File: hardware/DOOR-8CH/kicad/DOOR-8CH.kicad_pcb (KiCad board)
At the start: 4 copper layers, 260 x 160 mm, 209 parts, among them J1 FUSED_12V_CH1, J10 ACTUATOR_CH2, J11 ACTUATOR_CH3, J12 ACTUATOR_CH4, J13 ACTUATOR_CH5, J14 ACTUATOR_CH6, J15 ACTUATOR_CH7, J16 ACTUATOR_CH8, J2 FUSED_12V_CH2, J201 REED_A_OPEN_3V3_SIG_GND, J202 REED_A_CLOSED_3V3_SIG_GND, J203 REED_A_IN_PLACE_3V3_SIG_GND, J204 REED_B_OPEN_3V3_SIG_GND, J205 REED_B_CLOSED_3V3_SIG_GND, J206 REED_B_IN_PLACE_3V3_SIG_GND, J211 CAP_CS1_GND, J212 CAP_CS2_GND, J213 CAP_CS3_GND, J214 CAP_CS4_GND, J215 CAP_CS5_GND, J216 CAP_CS6_GND, J217 CAP_CS7_GND, J218 CAP_CS8_GND, J220 SWD_S1_3V3_DIO_CLK_NRST_GND, J230 LOGIC_12V_GND, J3 FUSED_12V_CH3, J4 FUSED_12V_CH4, J5 FUSED_12V_CH5, J6 FUSED_12V_CH6, J7 FUSED_12V_CH7, J8 FUSED_12V_CH8, J9 ACTUATOR_CH1, U1 VNH5019A-E, U2 VNH5019A-E, U3 VNH5019A-E, U4 VNH5019A-E, U5 VNH5019A-E, U6 VNH5019A-E, U7 VNH5019A-E, U8 VNH5019A-E

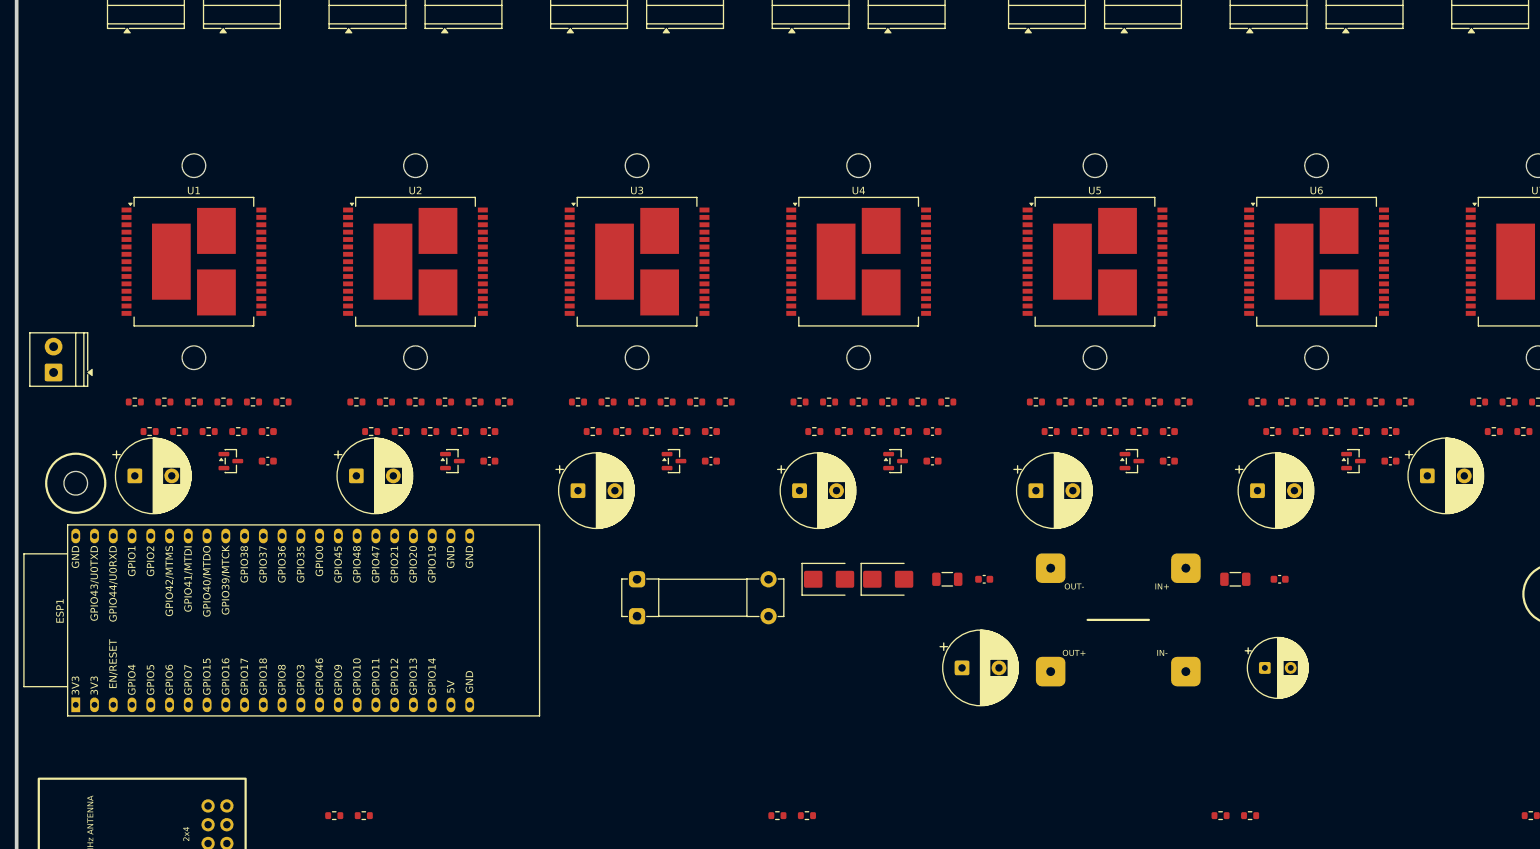
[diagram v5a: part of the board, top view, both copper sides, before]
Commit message: Add DOOR-8CH low-voltage nets
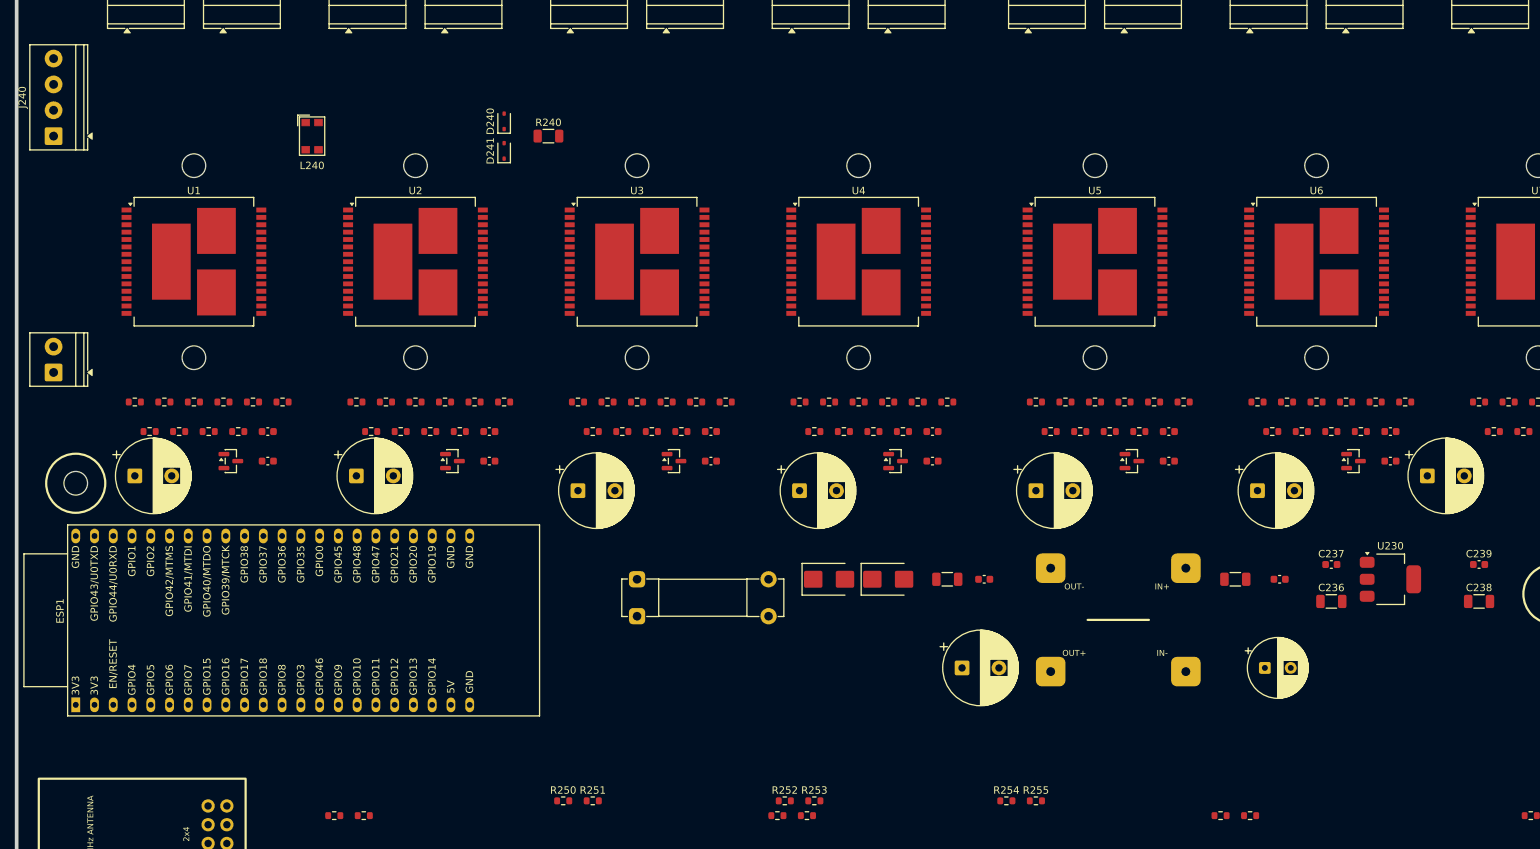
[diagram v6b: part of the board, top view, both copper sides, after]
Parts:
- added C236: 10UF_10V_3V3_IN, C_1206_3216Metric, F.Cu at (178.0, 91.0)
- added C237: 100NF_16V_3V3_IN, C_0603_1608Metric, F.Cu at (178.0, 86.0)
- added C238: 10UF_10V_3V3_OUT, C_1206_3216Metric, F.Cu at (198.0, 91.0)
- added C239: 100NF_16V_3V3_OUT, C_0603_1608Metric, F.Cu at (198.0, 86.0)
- added D240: PESD1CAN_CANH, D_SOD-323, F.Cu at (66.0, 26.0)
- added D241: PESD1CAN_CANL, D_SOD-323, F.Cu at (66.0, 30.0)
- added J240: CANH_CANL_GND_SHIELD, TerminalBlock_Phoenix_PT-1,5-4-3.5-H_1x04_P3.50mm_Horizontal, F.Cu at (5.00, 28.0)
- added L240: CMC_CAN, L_CommonModeChoke_Coilcraft_1812CAN, F.Cu at (40.0, 28.0)
- added R240: 120R_CAN_TERM_DNP, R_1206_3216Metric, F.Cu at (72.0, 28.0)
- added R250: 100R_UART_TX, R_0603_1608Metric, F.Cu at (74.0, 118.0)
- added R251: 100R_UART_TX, R_0603_1608Metric, F.Cu at (78.0, 118.0)
- added R252: 100R_UART_TX, R_0603_1608Metric, F.Cu at (104.0, 118.0)
- added R253: 100R_UART_TX, R_0603_1608Metric, F.Cu at (108.0, 118.0)
- added R254: 100R_UART_TX, R_0603_1608Metric, F.Cu at (134.0, 118.0)
- added R255: 100R_UART_TX, R_0603_1608Metric, F.Cu at (138.0, 118.0)
- added U230: AMS1117-3V3, SOT-223-3_TabPin2, F.Cu at (186.0, 88.0)
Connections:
- C230 pad 1: (no net) -> LOGIC_12V_PROTECTED
- C230 pad 2: (no net) -> GND
- C231 pad 1: (no net) -> LOGIC_12V_PROTECTED
- C231 pad 2: (no net) -> GND
- C232 pad 1: (no net) -> LOGIC_12V_PROTECTED
- C232 pad 2: (no net) -> GND
- C233 pad 1: (no net) -> LOGIC_5V
- C233 pad 2: (no net) -> GND
- C234 pad 1: (no net) -> LOGIC_5V
- C234 pad 2: (no net) -> GND
- C235 pad 1: (no net) -> LOGIC_5V
- C235 pad 2: (no net) -> GND
- CAN1 pad 1: (no net) -> LOGIC_3V3
- CAN1 pad 2: (no net) -> GND
- CAN1 pad 3: (no net) -> S1_CAN_TX
- CAN1 pad 4: (no net) -> S1_CAN_RX
- CAN1 pad 5: (no net) -> CANH_BUS
- CAN1 pad 6: (no net) -> CANL_BUS
- CAN2 pad 1: (no net) -> LOGIC_3V3
- CAN2 pad 2: (no net) -> GND
- CAN2 pad 3: (no net) -> ESP_CAN_TX_GPIO39
- CAN2 pad 4: (no net) -> ESP_CAN_RX_GPIO38
- CAN2 pad 5: (no net) -> CANH_BUS
- CAN2 pad 6: (no net) -> CANL_BUS
- CAP1 pad 1: (no net) -> CAP_MISO
- CAP1 pad 14: (no net) -> CAP_MOSI
- CAP1 pad 15: (no net) -> CAP_CS
- CAP1 pad 16: (no net) -> CAP_RESET
- CAP1 pad 18: (no net) -> CAP_C1_RAW
- CAP1 pad 19: (no net) -> CAP_C2_RAW
- CAP1 pad 2: (no net) -> CAP_SCK
- CAP1 pad 20: (no net) -> CAP_C3_RAW
- CAP1 pad 21: (no net) -> CAP_C4_RAW
- CAP1 pad 22: (no net) -> CAP_C5_RAW
- CAP1 pad 23: (no net) -> CAP_C6_RAW
- CAP1 pad 24: (no net) -> CAP_C7_RAW
- CAP1 pad 25: (no net) -> CAP_C8_RAW
- CAP1 pad 26: (no net) -> GND
- CAP1 pad 3: (no net) -> LOGIC_5V
- CAP1 pad 4: (no net) -> GND
- D230 pad 1: (no net) -> LOGIC_12V_FUSED
- D230 pad 2: (no net) -> LOGIC_12V_PROTECTED
- D231 pad 1: (no net) -> LOGIC_12V_PROTECTED
- D231 pad 2: (no net) -> GND
- DC1 pad 1: (no net) -> LOGIC_12V_PROTECTED
- DC1 pad 2: (no net) -> GND
- DC1 pad 3: (no net) -> LOGIC_5V
- DC1 pad 4: (no net) -> GND
- ESP1 pad 15: (no net) -> RF_LEARN_BUTTON_GPIO9
- ESP1 pad 16: (no net) -> RF_CSN
- ESP1 pad 17: (no net) -> RF_MOSI
- ESP1 pad 18: (no net) -> RF_SCK
- ESP1 pad 19: (no net) -> RF_MISO
- ESP1 pad 21: (no net) -> LOGIC_5V
- ESP1 pad 22: (no net) -> GND
- ESP1 pad 23: (no net) -> GND
- ESP1 pad 24: (no net) -> GND
- ESP1 pad 35: (no net) -> ESP_CAN_RX_GPIO38
- ESP1 pad 36: (no net) -> ESP_CAN_TX_GPIO39
- ESP1 pad 4: (no net) -> RF_GDO0
- ESP1 pad 44: (no net) -> GND
- ESP1 pad 5: (no net) -> RF_GDO2
- F230 pad 1: (no net) -> LOGIC_12V_IN
- F230 pad 2: (no net) -> LOGIC_12V_FUSED
- J201 pad 1: (no net) -> S1_3V3
- J201 pad 2: (no net) -> REED_A_OPEN
- J201 pad 3: (no net) -> GND
- J202 pad 1: (no net) -> S1_3V3
- J202 pad 2: (no net) -> REED_A_CLOSED
- J202 pad 3: (no net) -> GND
- J203 pad 1: (no net) -> S1_3V3
- J203 pad 2: (no net) -> REED_A_IN_PLACE
- J203 pad 3: (no net) -> GND
- J204 pad 1: (no net) -> S2_3V3
- J204 pad 2: (no net) -> REED_B_OPEN
- J204 pad 3: (no net) -> GND
- J205 pad 1: (no net) -> S2_3V3
- J205 pad 2: (no net) -> REED_B_CLOSED
- J205 pad 3: (no net) -> GND
- J206 pad 1: (no net) -> S2_3V3
- J206 pad 2: (no net) -> REED_B_IN_PLACE
- J206 pad 3: (no net) -> GND
- J211 pad 1: (no net) -> CAP_C1_FIELD
- J211 pad 2: (no net) -> GND
- J212 pad 1: (no net) -> CAP_C2_FIELD
- J212 pad 2: (no net) -> GND
- J213 pad 1: (no net) -> CAP_C3_FIELD
- J213 pad 2: (no net) -> GND
- J214 pad 1: (no net) -> CAP_C4_FIELD
- J214 pad 2: (no net) -> GND
- J215 pad 1: (no net) -> CAP_C5_FIELD
- J215 pad 2: (no net) -> GND
- J216 pad 1: (no net) -> CAP_C6_FIELD
- J216 pad 2: (no net) -> GND
- J217 pad 1: (no net) -> CAP_C7_FIELD
- J217 pad 2: (no net) -> GND
- J218 pad 1: (no net) -> CAP_C8_FIELD
- J218 pad 2: (no net) -> GND
- J220 pad 1: (no net) -> S1_3V3
- J220 pad 2: (no net) -> S1_SWDIO
- J220 pad 3: (no net) -> S1_SWCLK
- J220 pad 4: (no net) -> S1_NRST
- J220 pad 5: (no net) -> GND
- J230 pad 1: (no net) -> LOGIC_12V_IN
- J230 pad 2: (no net) -> GND
- MOD1 pad 13: (no net) -> CAP_IRQ
- MOD1 pad 14: (no net) -> S1_UART3_RX
- MOD1 pad 16: (no net) -> S1_NRST
- MOD1 pad 17: (no net) -> CAP_MISO
- MOD1 pad 18: (no net) -> CAP_CS
- MOD1 pad 19: (no net) -> S1_UART2_TX
- MOD1 pad 24: (no net) -> S1_CAN_TX
- MOD1 pad 25: (no net) -> S1_SWCLK
- MOD1 pad 28: (no net) -> S1_UART1_RX
- MOD1 pad 29: (no net) -> CAP_RESET
- MOD1 pad 33: (no net) -> S1_CAN_RX
- MOD1 pad 34: (no net) -> S1_SWDIO
- MOD1 pad 37: (no net) -> S1_UART1_TX
- MOD1 pad 38: (no net) -> REED_A_IN_PLACE
- MOD1 pad 4: (no net) -> S1_UART3_TX
- MOD1 pad 5: (no net) -> REED_A_CLOSED
- MOD1 pad 6: (no net) -> REED_A_OPEN
- MOD1 pad 7: S1_SLOT_ID1 -> CAP_MOSI
- MOD1 pad 8: (no net) -> CAP_SCK
- MOD1 pad 9: (no net) -> S1_UART2_RX
- MOD2 pad 28: (no net) -> S2_UART_RX
- MOD2 pad 37: (no net) -> S2_UART_TX
- MOD2 pad 38: (no net) -> REED_B_IN_PLACE
- MOD2 pad 5: (no net) -> REED_B_CLOSED
- MOD2 pad 6: (no net) -> REED_B_OPEN
- MOD3 pad 28: (no net) -> S3_UART_RX
- MOD3 pad 37: (no net) -> S3_UART_TX
- MOD4 pad 28: (no net) -> S4_UART_RX
- MOD4 pad 37: (no net) -> S4_UART_TX
- R201 pad 1: (no net) -> CAP_C1_RAW
- R201 pad 2: (no net) -> CAP_C1_FIELD
- R202 pad 1: (no net) -> CAP_C2_RAW
- R202 pad 2: (no net) -> CAP_C2_FIELD
- R203 pad 1: (no net) -> CAP_C3_RAW
- R203 pad 2: (no net) -> CAP_C3_FIELD
- R204 pad 1: (no net) -> CAP_C4_RAW
- R204 pad 2: (no net) -> CAP_C4_FIELD
- R205 pad 1: (no net) -> CAP_C5_RAW
- R205 pad 2: (no net) -> CAP_C5_FIELD
- R206 pad 1: (no net) -> CAP_C6_RAW
- R206 pad 2: (no net) -> CAP_C6_FIELD
- R207 pad 1: (no net) -> CAP_C7_RAW
- R207 pad 2: (no net) -> CAP_C7_FIELD
- R208 pad 1: (no net) -> CAP_C8_RAW
- R208 pad 2: (no net) -> CAP_C8_FIELD
- R209 pad 1: (no net) -> CAP_RESET
- R209 pad 2: (no net) -> GND
- R210 pad 1: (no net) -> CAP_IRQ
- R210 pad 2: (no net) -> S1_3V3
- RF1 pad 1: (no net) -> RF_GDO0
- RF1 pad 2: (no net) -> LOGIC_3V3
- RF1 pad 3: (no net) -> RF_CSN
- RF1 pad 4: (no net) -> GND
- RF1 pad 5: (no net) -> RF_SCK
- RF1 pad 6: (no net) -> RF_MOSI
- RF1 pad 7: (no net) -> RF_MISO
- RF1 pad 8: (no net) -> RF_GDO2

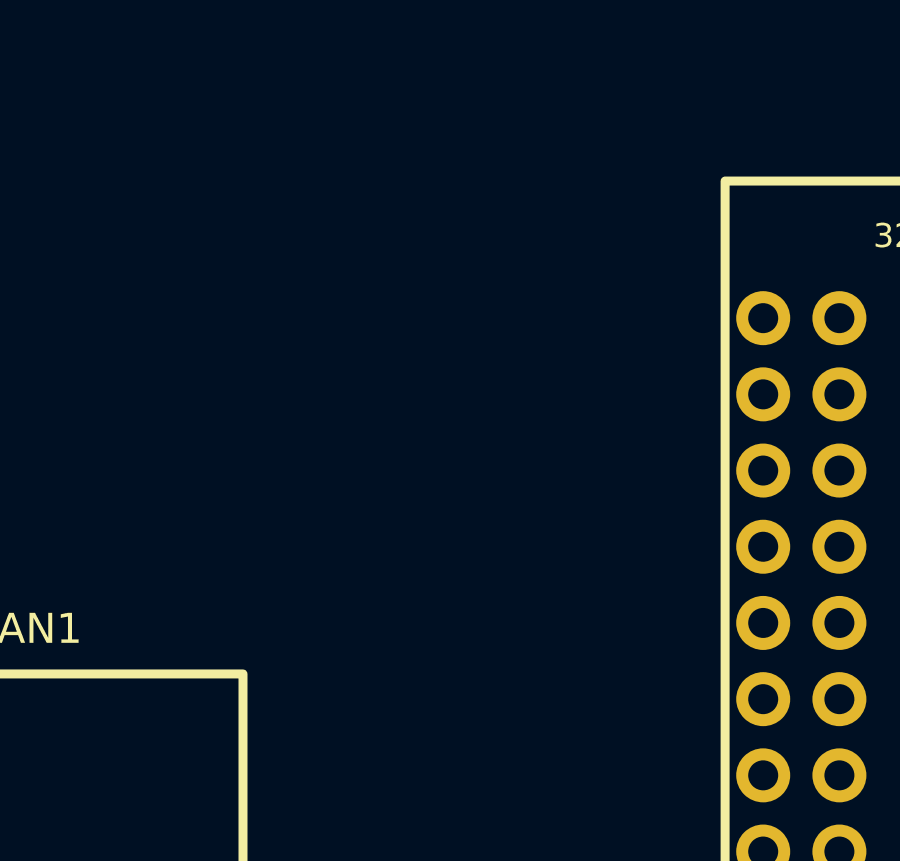
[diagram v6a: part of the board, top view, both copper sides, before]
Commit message: Add carrier EEPROM support
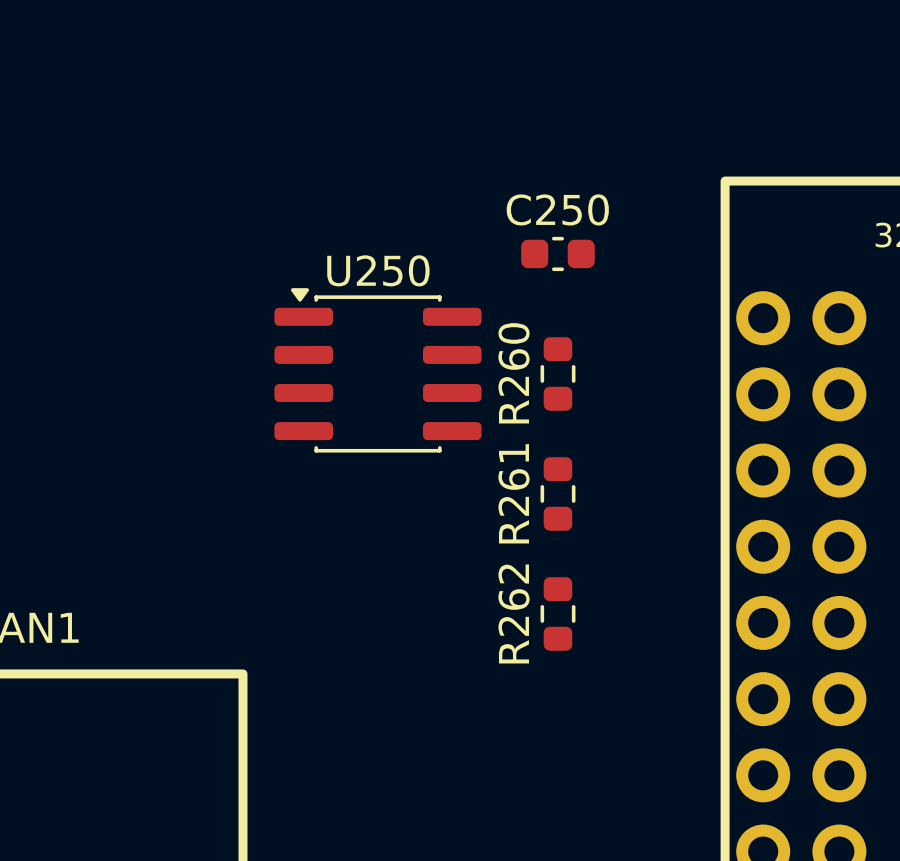
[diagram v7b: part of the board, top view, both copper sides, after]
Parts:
- added C250: 100NF_EEPROM, C_0603_1608Metric, F.Cu at (88.0, 128.0)
- added R260: 10K_EEPROM_CS_PULLUP, R_0603_1608Metric, F.Cu at (88.0, 132.0)
- added R261: 10K_EEPROM_WP_PULLUP, R_0603_1608Metric, F.Cu at (88.0, 136.0)
- added R262: 10K_EEPROM_HOLD_PULLUP, R_0603_1608Metric, F.Cu at (88.0, 140.0)
- added U250: 25LC256_SOIC8_CARRIER_ID, SOIC-8_3.9x4.9mm_P1.27mm, F.Cu at (82.0, 132.0)
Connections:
- MOD1 pad 35: (no net) -> EEPROM_CS
